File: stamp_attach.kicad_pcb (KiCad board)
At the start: 2 copper layers, 90 x 74 mm, 23 parts, among them J1 SA_layer_A, J2 SA_layer_D

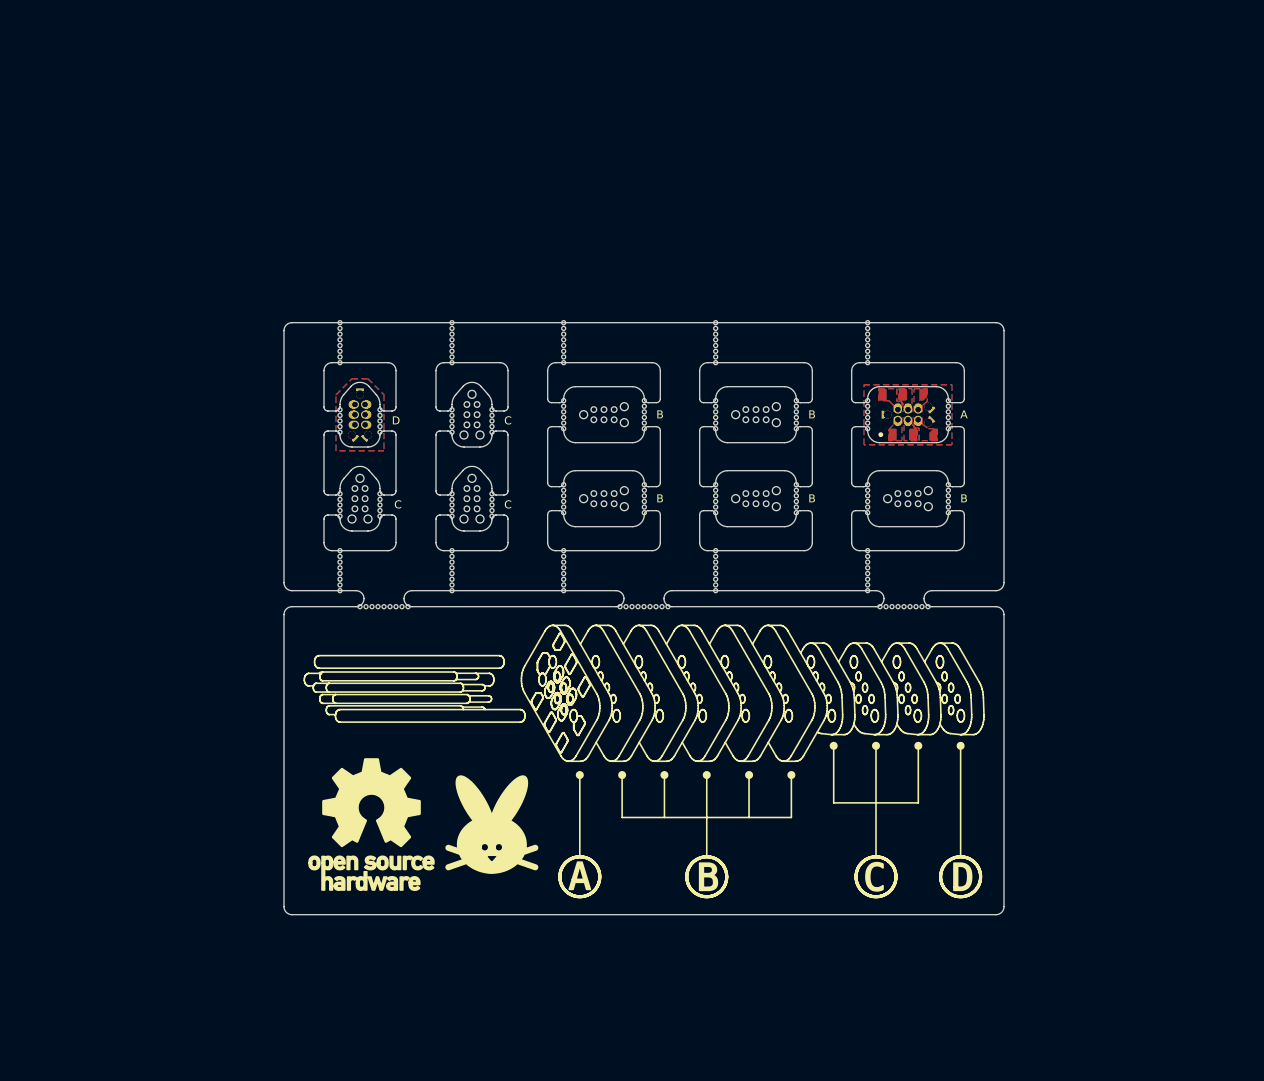
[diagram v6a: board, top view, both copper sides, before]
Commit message: completed graphics area of info card
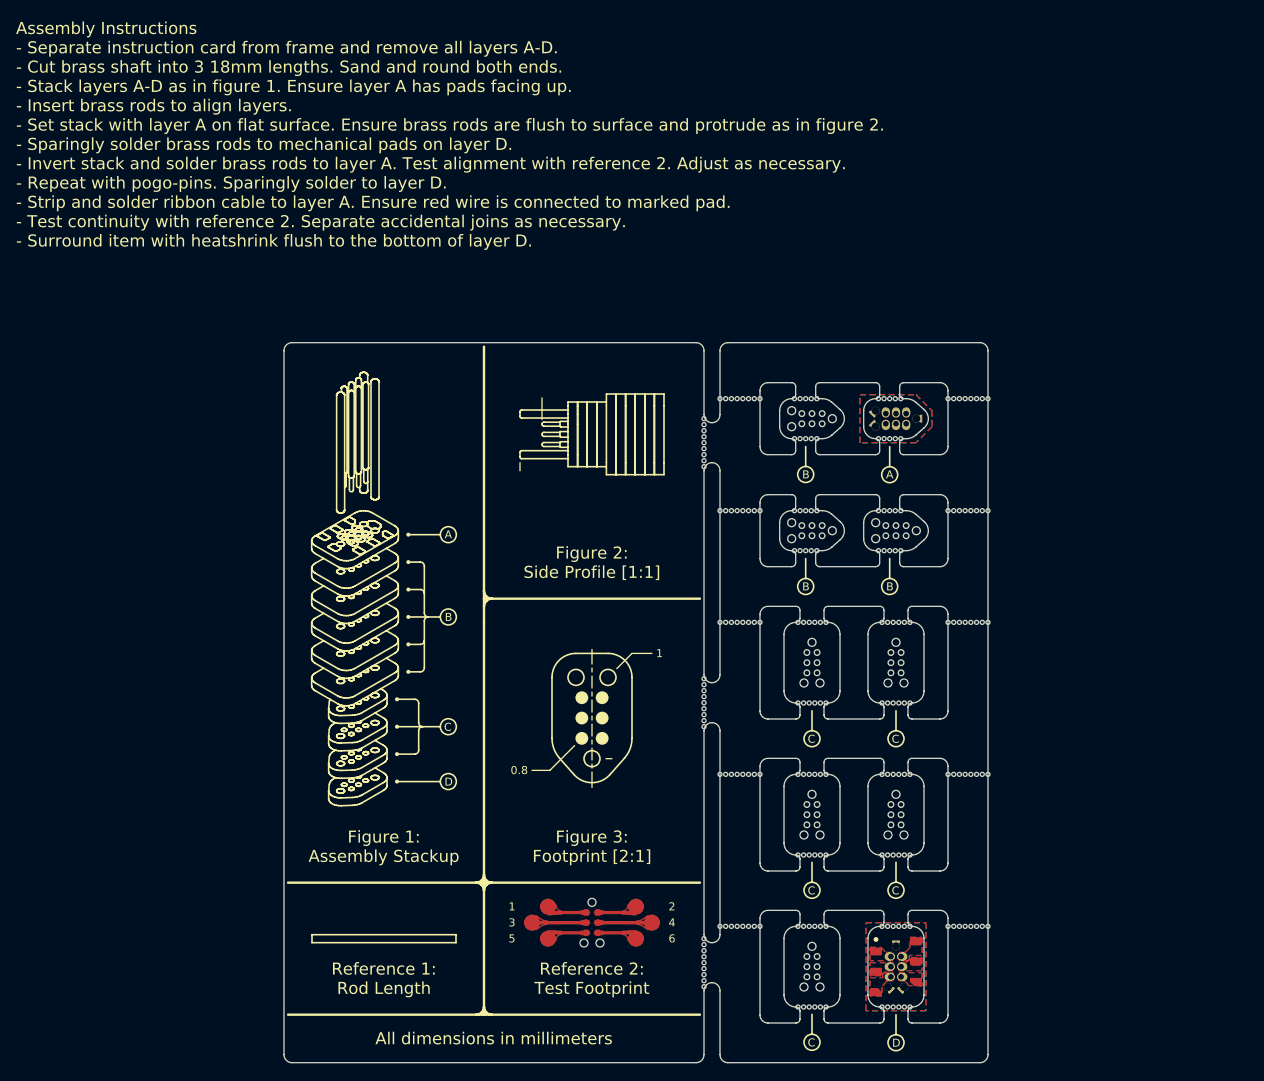
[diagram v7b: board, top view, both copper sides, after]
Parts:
- added J3: test_footprint, Stamp_Attach:Test_Footprint, F.Cu at (143.5, 130.0)
- moved REF** 78.8 mm to (190.5, 64.5), turned to 0 degrees
- moved REF** 74.0 mm to (190.5, 130.5), turned to 0 degrees
- moved J1 69.0 mm to (181.5, 135.5), turned to -90 degrees
- moved REF** 67.8 mm to (190.5, 78.5), turned to 0 degrees
- moved J2 67.0 mm to (181.5, 67.0), turned to 180 degrees
- moved REF** 62.5 mm to (190.5, 111.5), turned to 0 degrees
- moved REF** 61.5 mm to (190.5, 92.5), turned to 0 degrees
- moved REF** 59.7 mm to (171.0, 135.5), turned to -90 degrees
- moved REF** 57.4 mm to (171.0, 67.0), turned to 180 degrees
- moved REF** 54.9 mm to (181.5, 81.0), turned to 180 degrees
- moved REF** 54.4 mm to (162.0, 64.5), turned to 0 degrees
- moved REF** 53.0 mm to (181.5, 116.5), turned to -90 degrees
- moved REF** 51.4 mm to (158.5, 135.0), turned to -90 degrees
- moved REF** 47.9 mm to (181.5, 97.5), turned to -90 degrees
- moved REF** 47.2 mm to (162.0, 130.5), turned to 0 degrees
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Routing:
- net unconnected-(J3-Pad4): track 0.00 -> 6.87 mm
- net unconnected-(J3-Pad3): track 0.00 -> 6.87 mm
- net unconnected-(J3-Pad6): track 0.00 -> 5.17 mm
- net unconnected-(J3-Pad5): track 0.00 -> 5.17 mm
- net unconnected-(J3-Pad2): track 0.00 -> 5.17 mm
- net unconnected-(J3-Pad1): track 0.00 -> 5.17 mm
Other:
- board size 90 x 74 mm -> 88 x 90 mm
- board text added: "0.8"
- board text added: "1"
- board text added: "2"
- board text added: "3"
- board text added: "4"
- board text added: "5"
- board text added: "6"
- board text added: "All dimensions in millimeters"
- board text added: "Assembly Instructions - Separate instruction card from frame and remove all layers A-D. - Cut brass shaft into 3 18mm lengths. Sand and round both ends. - Stack layers A-D as in figure 1. Ensure layer A has pads facing up. - Insert brass rods to align layers. - Set stack with layer A on flat surface. Ensure brass rods are flush to surface and protrude as in figure 2. - Sparingly solder brass rods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"
- board text added: "Figure 1: Assembly Stackup"
- board text added: "Figure 2: Side Profile [1:1]"
- board text added: "Figure 3: Footprint [2:1]"
- board text added: "Reference 1: Rod Length"
- board text added: "Reference 2: Test Footprint"

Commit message: Added instruction text
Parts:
- added REF**: OSHW-Symbol_6.7x6mm_SilkScreen, Symbol:OSHW-Symbol_6.7x6mm_SilkScreen, B.Cu at (151.8, 64.0)
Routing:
- added copper zone on B.Cu, net (none)
- added copper zone on F.Cu, net (none)
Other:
- board text added: "- Brass rods and pogo pins should be flush to layer A. - Solder sparingly on layer D to ensure clearance and fitment. - Use reference 2 to test alignment of rods and continuity."
- board text added: "- Separate instruction card from frame and remove all layers A-D. - Cut brass shaft into 3 18mm lengths. Sand and round both ends. - Stack layers A-D as in figure 1. Ensure layer A has pads facing up. - Insert brass rods as per figure 2. Solder to layers A and D. - Repeat with with pogo-pins in remaining holes. - Attach desired cable to pads on layer A. Finish with heatshrink."
- board text added: "Assembly Instructions"
- board text added: "JLCJLCJLCJLC"
- board text added: "Stamp-Attach"
- board text added: "Tips"
- board text added: "Use figure 3 to replicate the recipient footprint in your EDA suite."
- board text removed: "Assembly Instructions - Separate instruction card from frame and remove all layers A-D. - Cut brass shaft into 3 18mm lengths. Sand and round both ends. - Stack layers A-D as in figure 1. Ensure layer A has pads facing up. - Insert brass rods to align layers. - Set stack with layer A on flat surface. Ensure brass rods are flush to surface and protrude as in figure 2. - Sparingly solder brass rods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"
